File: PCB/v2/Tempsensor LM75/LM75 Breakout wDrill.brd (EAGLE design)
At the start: 37.5 x 12.1 mm, 6 parts

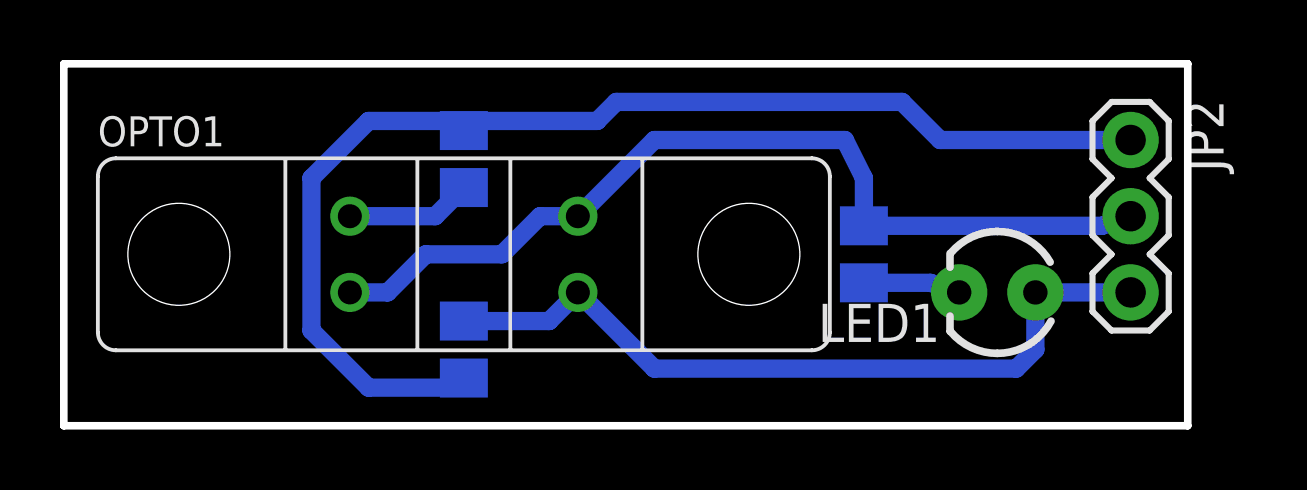
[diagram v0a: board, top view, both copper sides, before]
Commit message: -add two new version of SatNogs Board (combined PSU+Arduino board) -add new end stop (v2), add TSTC2103 signal amplifier -move extend library to include all board elements, update elements, include satnogs logo -include reference datasheets document, design rule files -move current design into v1 directory, show board dimension, export schematic and board as pdf
Combined commits:

remove Datasheets, include a Markdown document instead (possible legal issues)

satnogs_board: cleanup spice simulations, add result png

satnogs_board: include pdfs of schematic/board

include operational amplifier circuit for position sensing (potentiometric)

include TS912 opamp device and datasheet

library add discharge tube
finalize v2 board

include gas discharge tube

add LM75 breakouts
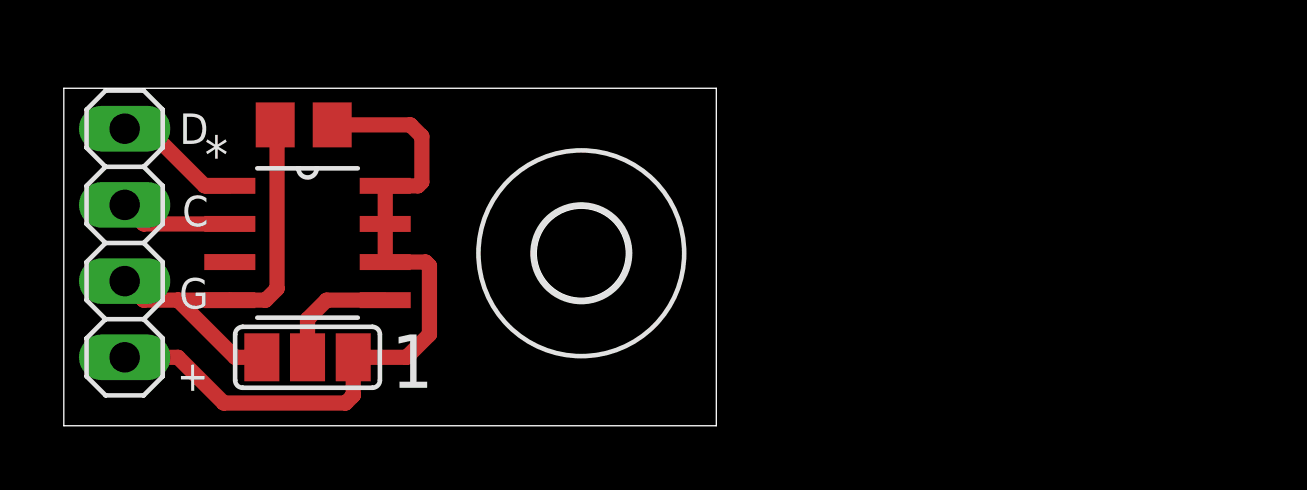
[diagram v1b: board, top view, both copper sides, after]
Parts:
- removed JP2: (no value), SparkFun-Connectors:1X03
- removed LED1: (no value), SparkFun-LED:LED3MM
- removed OPTO1: TCST2103, satnogs:TCST2013
- removed R1: 180, rcl:M0805
- removed R2: 150, rcl:M0805
- removed R3: 2k2, rcl:M0805
- added A0$1: (no value), jumper:SJ_2
- added C1: 100nF, rcl:C0805
- added JP1: (no value), pinhead:1X04
- added U$1: (no value), holes:3,0
- added U1: LM75BD, NXP_By_element14_Batch_1:SOIC127P600X175-8N
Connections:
- removed net N$2: OPTO1.LED_A, R1.1
- removed net N$7: LED1.K, R2.2
- removed net SIGNAL: JP2.3, LED1.A, OPTO1.NPN_C, R3.1
- removed net VCC: JP2.1, R1.2, R3.2
- new net +5V: A0$1.3, C1.1, JP1.1, U1.6, U1.7, U1.8
- new net I2C_SCL: JP1.3, U1.2
- new net I2C_SDA: JP1.4, U1.1
- new net N$1: A0$1.2, U1.5
- net GND: now also A0$1.1, C1.2, JP1.2, U1.4; no longer JP2.2, OPTO1.LED_K, OPTO1.NPN_E, R2.1
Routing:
- net VCC: track 40.7 -> 0.00 mm
- net SIGNAL: track 25.8 -> 0.00 mm
- net +5V: track 0.00 -> 24.8 mm
- net GND: track 30.6 -> 14.6 mm
- net I2C_SDA: track 0.00 -> 4.29 mm
- net N$2: track 4.20 -> 0.00 mm
- net N$1: track 0.00 -> 4.12 mm
- net I2C_SCL: track 0.00 -> 3.77 mm
- net N$7: track 3.23 -> 0.00 mm
- removed copper zone on layer 16, net GND
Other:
- board size 37.5 x 12.1 mm -> 21.8 x 11.2 mm
- board text added: "1"
- board text added: "D C G +"
- board text removed: "+5V"
- board text removed: "GND"
- board text removed: "SatNOGS"
